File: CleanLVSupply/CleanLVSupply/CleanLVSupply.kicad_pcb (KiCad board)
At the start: 4 copper layers, 40 x 40 mm, 76 parts, among them J1 12VIN, J2 +-15V, J3 +-15V, J4 5V, J5 5V, J6 5V, U1 LM25576, U2 TPS7A30, U3 LMR64010XMF, U4 TPS7A47, U5 LMR54406F, U6 TPS7A47

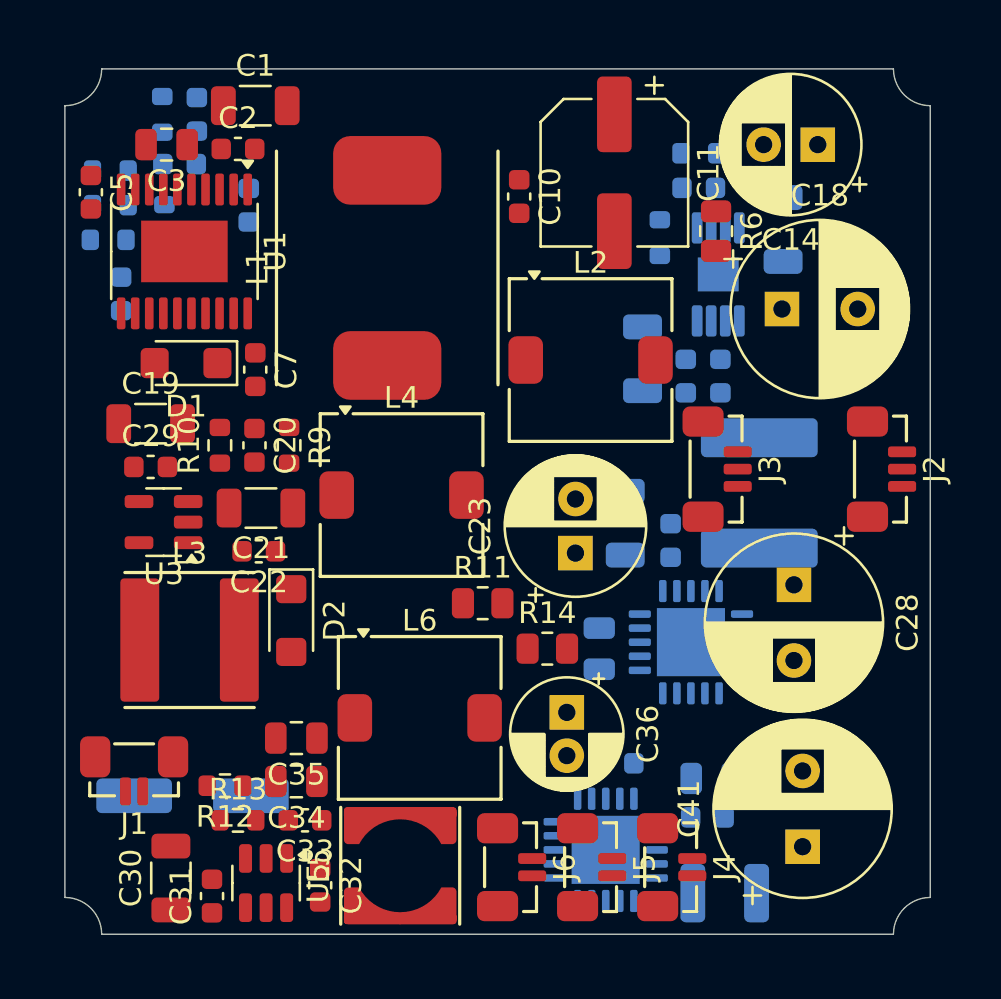
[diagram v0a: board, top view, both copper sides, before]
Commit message: CleanLVSupply routing progress
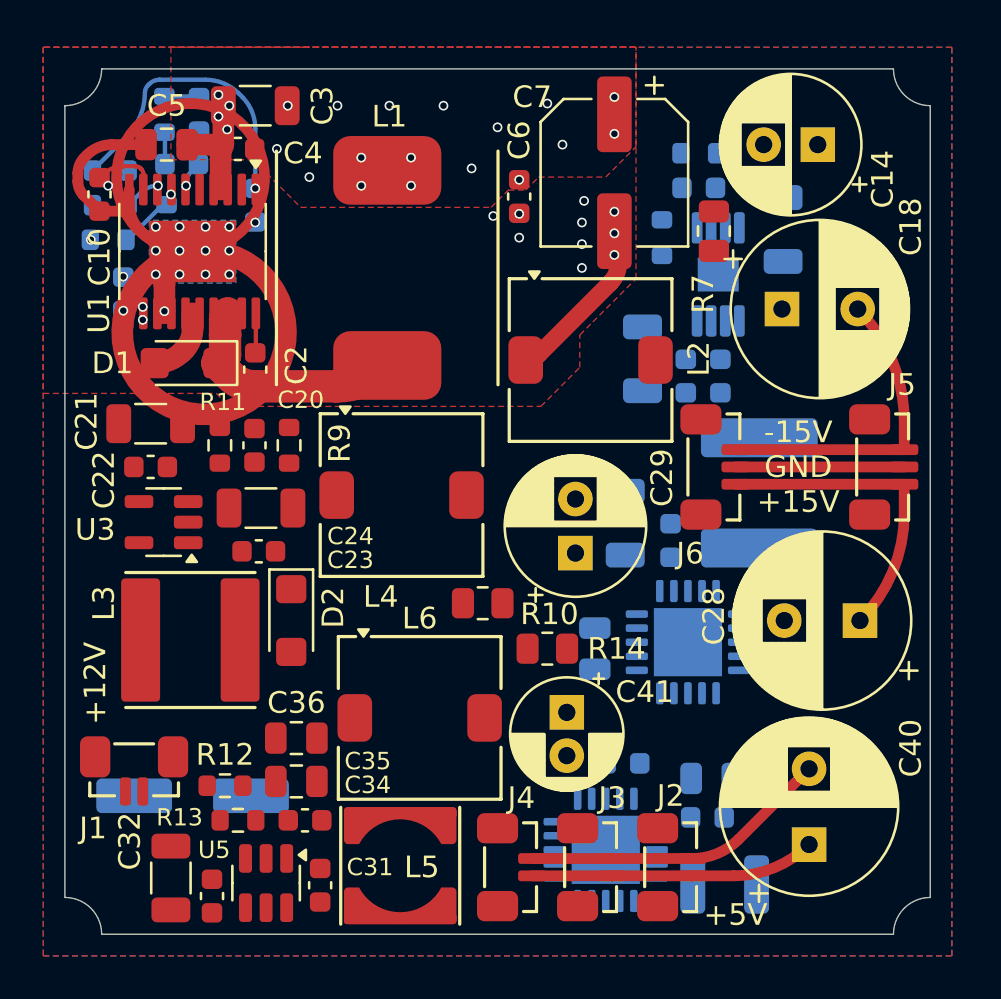
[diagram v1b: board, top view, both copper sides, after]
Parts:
- moved C28 3.47 mm to (166.8, 105.5), turned to 180 degrees
- moved C10 0.41 mm to (131.6, 85.8)
- moved C39 0.40 mm to (160.5, 117.7)
- moved U1 0.38 mm to (135.9, 88.4)
- moved C40 0.32 mm to (164.4, 115.9)
- moved C9 0.30 mm to (138.8, 86.3)
- moved C42 0.28 mm to (155.8, 112.1)
- moved C30 0.20 mm to (154.5, 106.8)
- moved J5 0.14 mm to (167.8, 98.4)
- moved J6 0.14 mm to (160.0, 98.4)
- moved U4 0.14 mm to (158.8, 106.5)
- moved C11 0.10 mm to (132.7, 90.4)
- moved C12 0.10 mm to (135.4, 84.4)
- moved C8 0.10 mm to (136.2, 82.1)
- moved R3 0.10 mm to (134.6, 82.1)
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- renumbered C42 to C1, C5 to C10, C6 to C11, C9 to C12, C15 to C13, C13 to C15, C12 to C16, C16 to C19, C7 to C2, C19 to C21, C29 to C22, C22 to C23, C21 to C24, C24 to C25, C25 to C26, C23 to C29, C1 to C3, C26 to C30, C32 to C31, C30 to C32, C31 to C33, C33 to C34, C34 to C35, C35 to C36, C40 to C39, C2 to C4, C41 to C40, C36 to C41, C39 to C42, C3 to C5, C10 to C6, C11 to C7, C4 to C9, J4 to J2, J5 to J3, J6 to J4, J2 to J5, J3 to J6, R3 to R1, R11 to R10, R10 to R11, R1 to R2, R5 to R3, R2 to R4, R4 to R5, R8 to R6, R6 to R7, R7 to R8
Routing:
- net /-15V Supply/-17V_SW: track 0.00 -> 27.8 mm, vias 0 -> 25
- net GND: track 0.00 -> 22.2 mm, vias 0 -> 20
- net -15V: track 0.00 -> 14.8 mm
- net +15V: track 0.00 -> 14.6 mm
- net Net-(U1-VCC): track 0.00 -> 13.9 mm, vias 0 -> 1
- net +5V: track 0.00 -> 13.2 mm
- net Net-(D1-K): track 0.00 -> 12.2 mm
- net Net-(U1-FB): track 0.00 -> 6.23 mm, vias 0 -> 1
- net +12V: track 0.00 -> 6.18 mm, vias 0 -> 4
- net Net-(U1-RAMP): track 0.00 -> 4.84 mm, vias 0 -> 1
- net Net-(D1-A): track 0.00 -> 3.96 mm
- net Net-(U1-COMP): track 0.00 -> 2.91 mm, vias 0 -> 1
- net Net-(U1-RT): track 0.00 -> 1.88 mm, vias 0 -> 1
- net Net-(U1-BST): track 0.00 -> 1.83 mm
- net Net-(C8-Pad2): track 0.00 -> 1.61 mm
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- added copper zone on B.Cu, net /-15V Supply/-17V_SW
- added copper zone on F.Cu, net /-15V Supply/-17V_SW
- added copper zone on In1.Cu, net /-15V Supply/-17V_SW
- added copper zone on B.Cu, net GND
- added copper zone on F.Cu, net GND
- added copper zone on In1.Cu, net GND
- added copper zone on In2.Cu, net GND
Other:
- board text added: "+12V"
- board text added: "+5V"
- board text added: "-15V GND +15V"

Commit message: CleanLVSupply design done for now
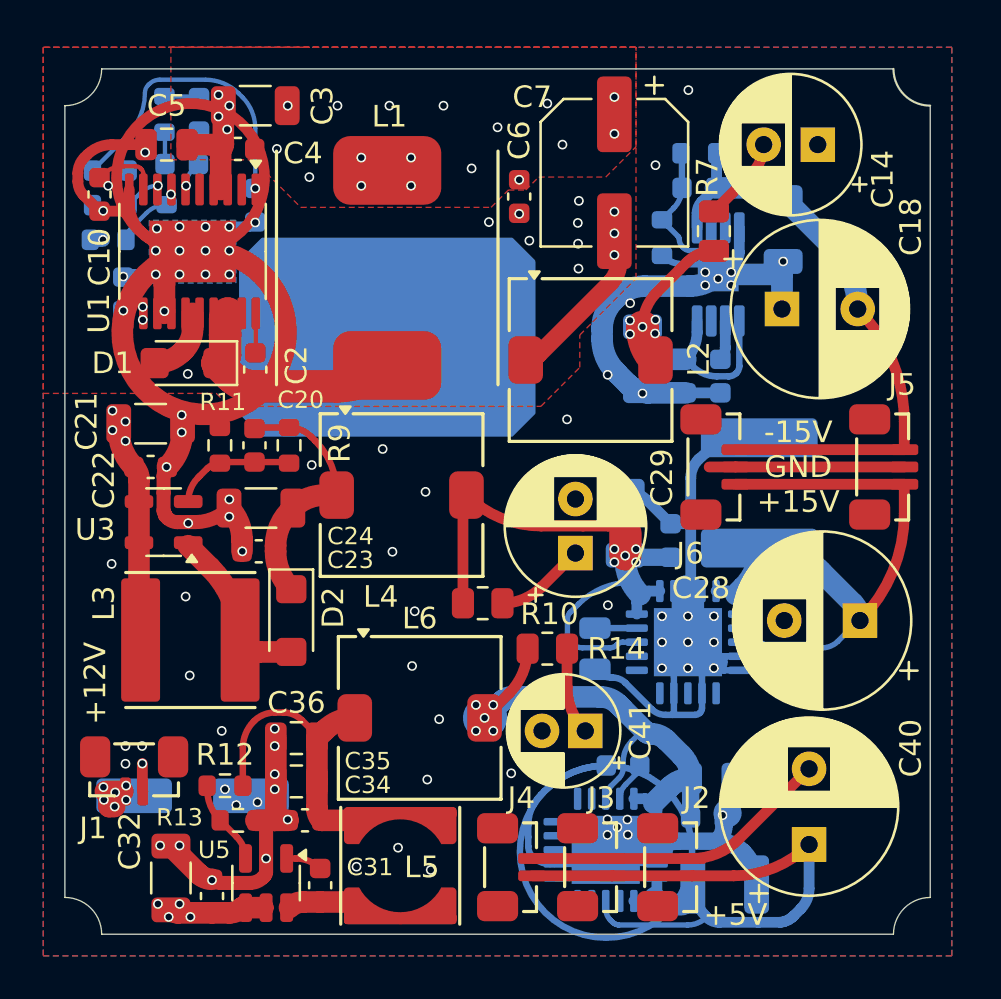
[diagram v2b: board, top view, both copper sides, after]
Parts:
- added REF**: BW_Logo_12.5x8mm, BW_Logo:BW_Logo_12.5x8mm, B.Cu at (144.9, 92.4)
- moved C41 1.21 mm to (154.1, 110.6), turned to 180 degrees
- moved C42 0.10 mm to (155.8, 112.2)
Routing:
- net GND: track 22.2 -> 138.4 mm, vias 20 -> 88
- net Net-(U4-EN): track 0.00 -> 27.7 mm, vias 0 -> 5
- net Net-(U6-EN): track 0.00 -> 25.2 mm, vias 0 -> 5
- net +5V: track 13.2 -> 32.5 mm
- net Net-(U2-EN): track 0.00 -> 16.8 mm, vias 0 -> 5
- net +15V: track 14.6 -> 31.2 mm
- net +12V: track 6.18 -> 22.7 mm, vias 4 -> 18
- net /5V Supply/7V_SW: track 0.00 -> 16.2 mm
- net -15V: track 14.8 -> 28.2 mm
- net Net-(D2-K): track 0.00 -> 12.1 mm
- net Net-(D2-A): track 0.00 -> 7.82 mm
- net Net-(U2-FB): track 0.00 -> 7.17 mm
- net Net-(U3-FB): track 0.00 -> 5.69 mm
- net Net-(U5-SW): track 0.00 -> 5.51 mm
- net Net-(C29-Pad1): track 0.00 -> 4.21 mm
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- added copper zone on In1.Cu, net +12V
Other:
- rule pad_to_mask_clearance: 0.038 -> 0
- board text added: "Modular Audio Clean LV Supply"
